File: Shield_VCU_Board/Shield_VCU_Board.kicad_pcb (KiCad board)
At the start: 2 copper layers, 250.5 x 110 mm, 148 parts, among them J1 Conn_02x08_Odd_Even, J10 Main_Supply, J11 Conn_01x40_Socket, J13 Conn_Molex_TouchPanel, J14 CAN_OUT, J15 Conn_01x04_Socket, J2 Conn_02x10_Odd_Even, J3/1 NXP3, J4 Conn_02x08_Odd_Even, J5 Conn_02x10_Odd_Even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

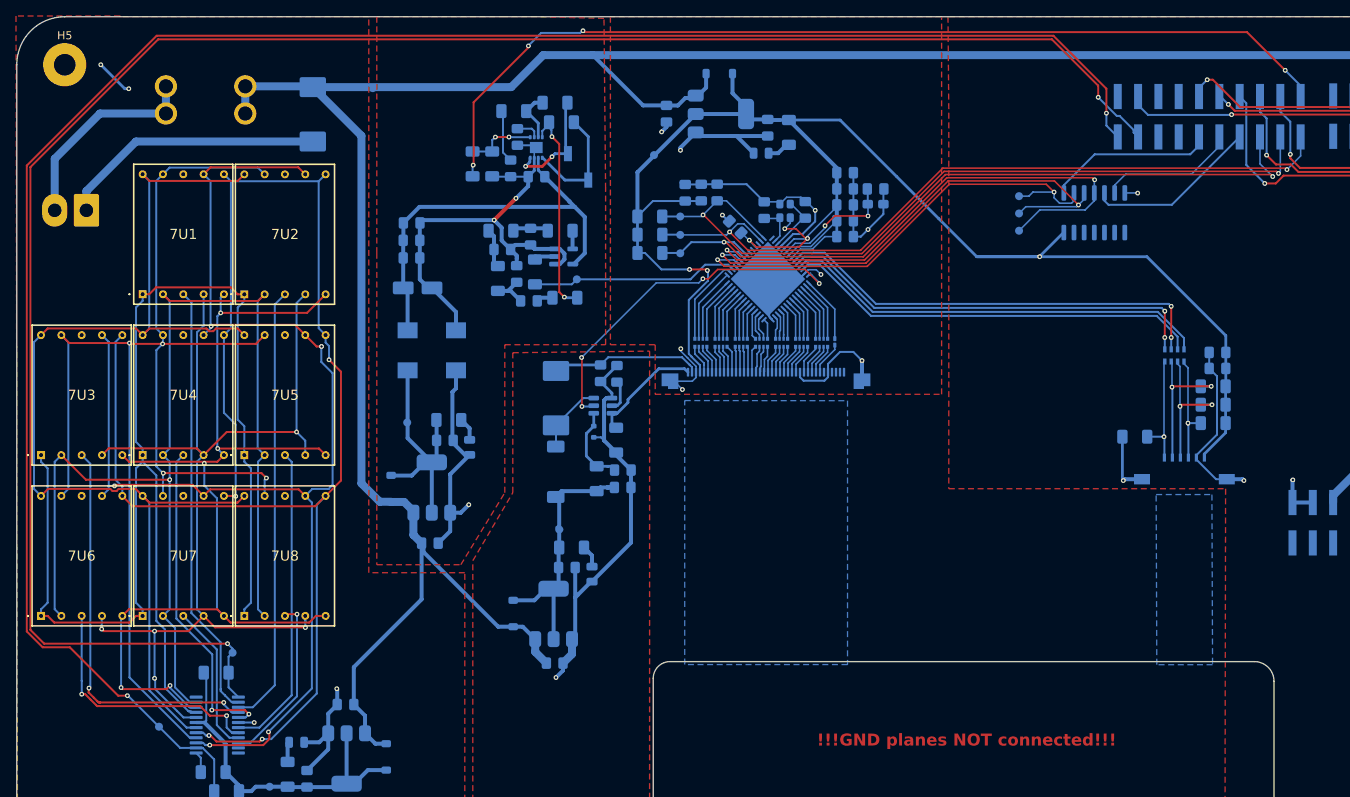
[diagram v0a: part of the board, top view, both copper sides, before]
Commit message: Wire routing_small change
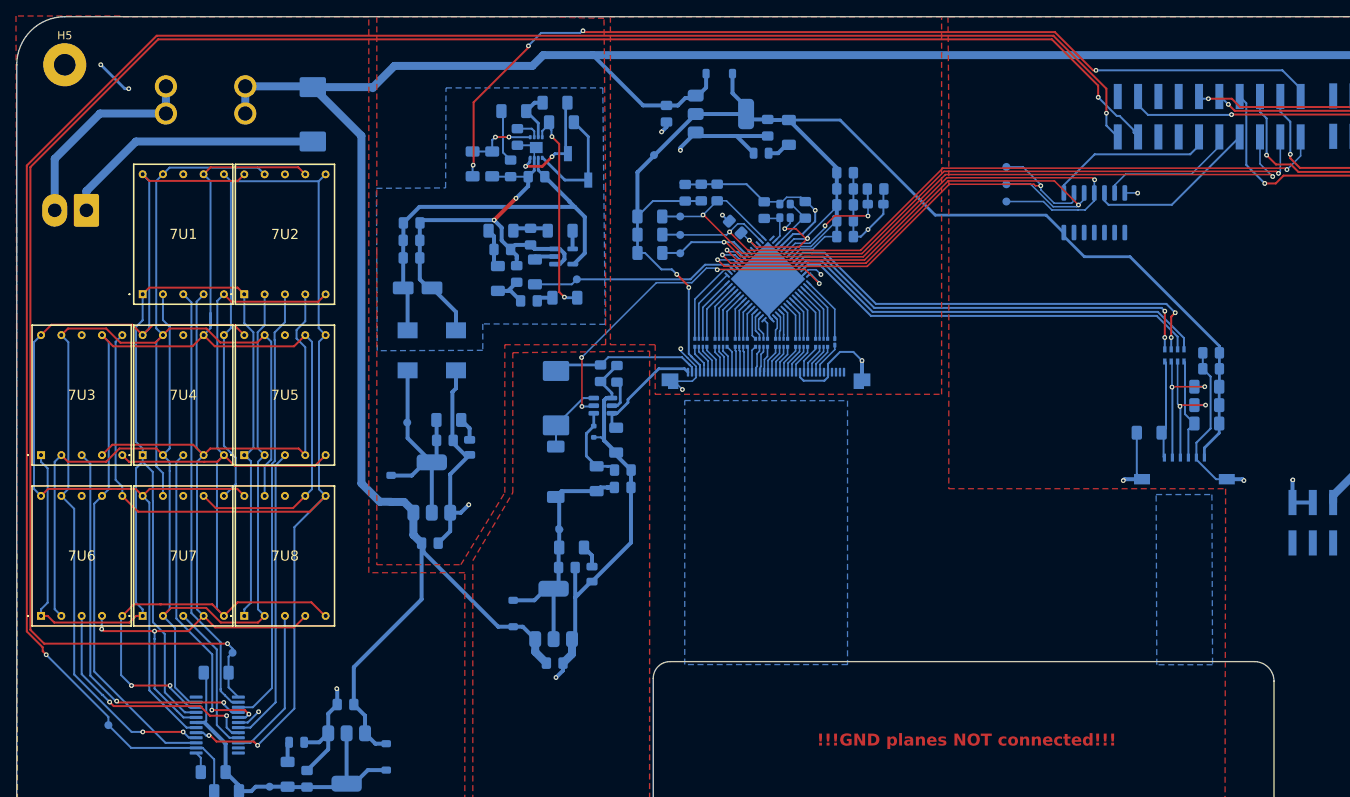
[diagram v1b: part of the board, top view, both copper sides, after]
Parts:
- moved SCL7 6.33 mm to (36.5, 132.6)
- moved MISO1 3.98 mm to (148.7, 64.9)
- moved MOSI1 3.98 mm to (148.7, 67.1)
- moved SCK1 3.98 mm to (148.7, 62.8)
- moved R62 1.87 mm to (166.6, 96.0)
- moved C16 0.80 mm to (174.3, 86.0)
- moved C41 0.80 mm to (174.3, 88.0)
- moved R61 0.80 mm to (173.8, 94.8)
- moved R63 0.80 mm to (173.8, 92.5)
- moved R64 0.80 mm to (173.8, 90.2)
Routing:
- net 3V3_DSPL: track 222.5 -> 204.2 mm, vias 6 -> 5
- net Net-(7U1-F): track 170.9 -> 166.5 mm, vias 4 -> 2
- net Net-(7U1-A): track 160.5 -> 158.0 mm, vias 5 -> 0
- net Net-(U1-DIG7): track 21.6 -> 19.2 mm, vias 1 -> 0
- net FT_MISO: track 62.8 -> 65.2 mm
- net Net-(J2-Pin_12): track 172.4 -> 170.1 mm
- net Net-(J13-Pin_6): track 14.2 -> 12.4 mm, vias 1 -> 0
- net Net-(U1-DIG2): track 50.1 -> 48.6 mm
- net Net-(U1-DIG5): track 32.3 -> 30.9 mm
- net Net-(7U1-B): track 187.0 -> 185.6 mm, vias 4 -> 2
- net Net-(U1-DIG4): track 38.7 -> 37.3 mm
- net GND: track 295.3 -> 296.6 mm
- net Net-(J13-Pin_3): track 13.8 -> 12.9 mm, vias 1 -> 0
- net FT_MOSI: track 67.0 -> 67.9 mm
- net 7S_NXP_SCL: track 244.7 -> 245.6 mm
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- added copper zone on B.Cu, net GNDA

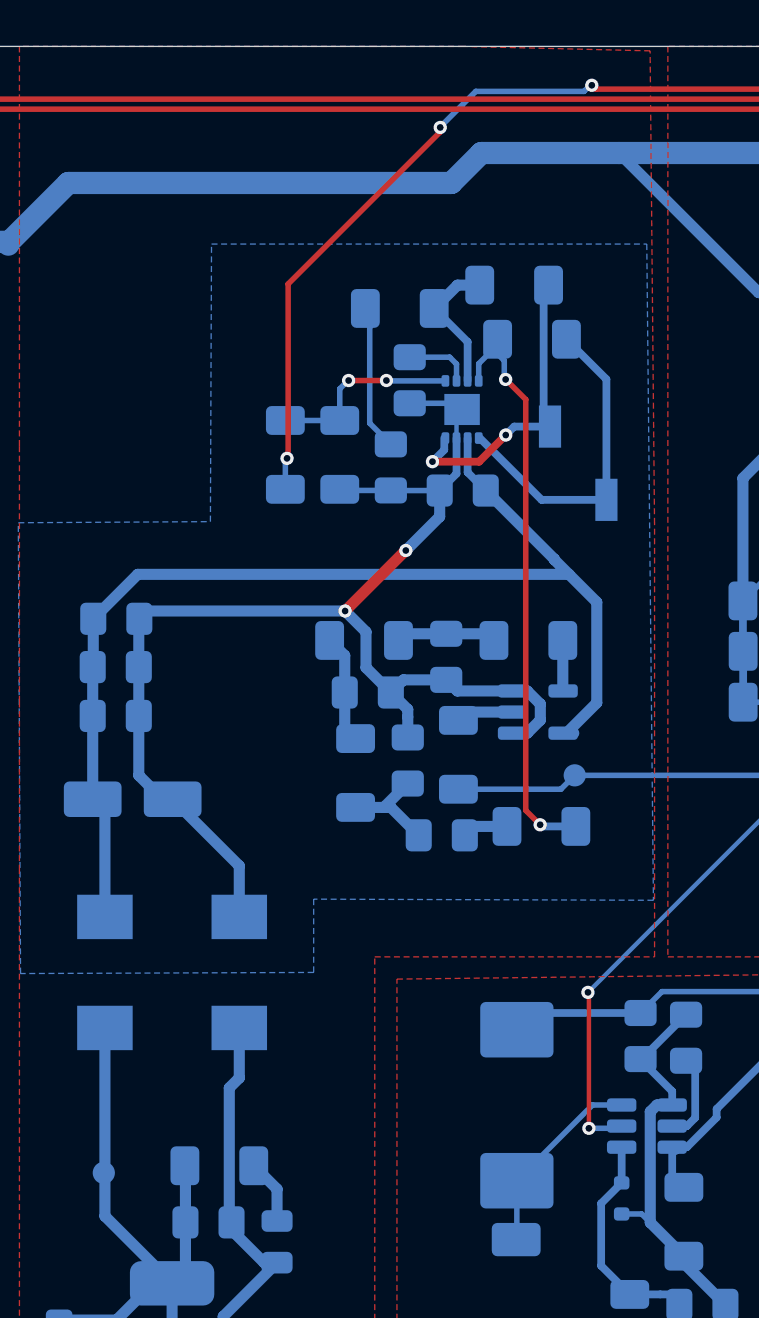
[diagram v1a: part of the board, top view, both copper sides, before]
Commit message: GNDA plane added(proto)
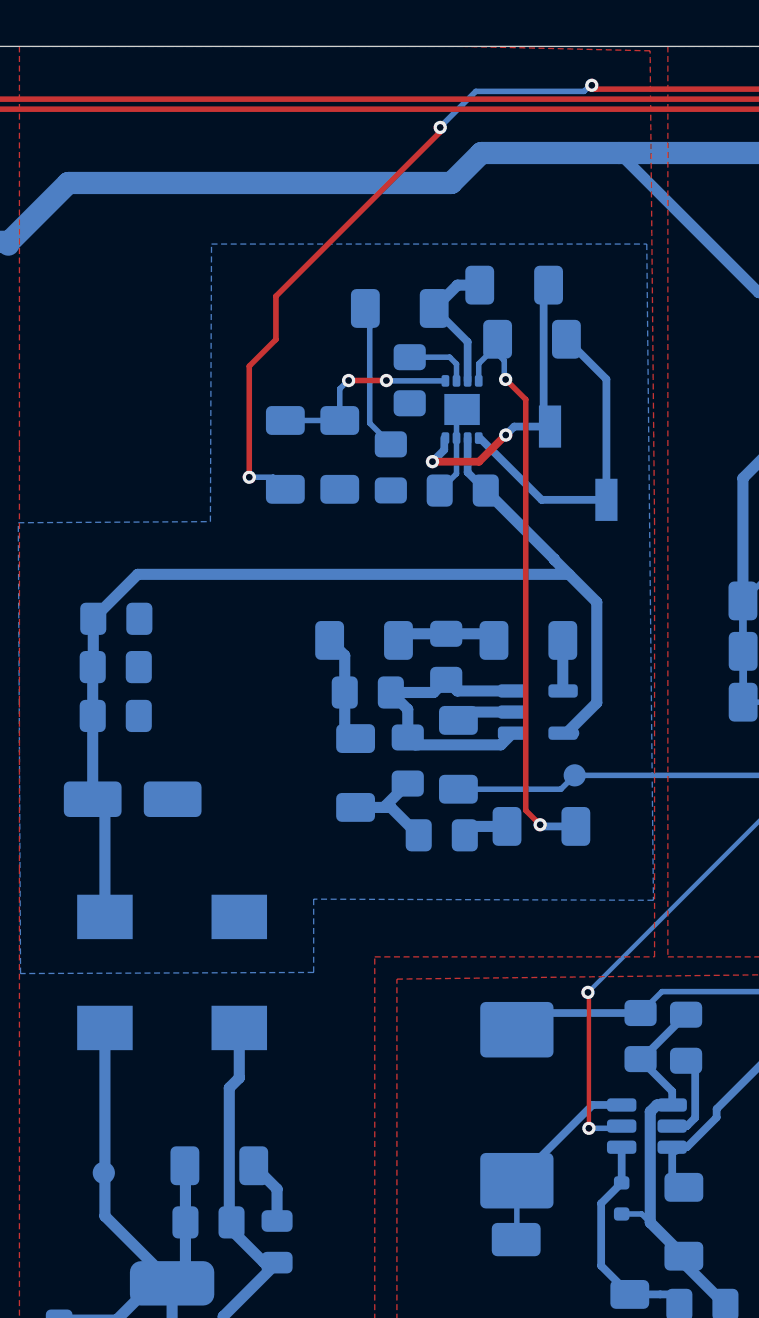
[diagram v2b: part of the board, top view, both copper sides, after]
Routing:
- net GNDA: track 60.7 -> 17.4 mm, vias 2 -> 0
- net AUD_SHDN: track 120.7 -> 122.7 mm

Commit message: Audio rotate+ GNDA plane separate
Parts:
- moved J8 13.4 mm to (82.8, 67.9), turned to 0 degrees
- moved R13 10.4 mm to (90.8, 65.0), turned to 90 degrees
- moved R8 10.2 mm to (87.3, 80.8), turned to 90 degrees
- moved R15 9.87 mm to (88.3, 65.8), turned to 90 degrees
- moved C11 9.49 mm to (82.0, 75.4), turned to 90 degrees
- moved R9 9.31 mm to (93.3, 81.2), turned to 180 degrees
- moved C2 8.54 mm to (89.7, 80.7), turned to 90 degrees
- moved C6 8.54 mm to (81.5, 62.7), turned to -90 degrees
- moved R10 7.75 mm to (83.1, 54.7), turned to 180 degrees
- moved C42 7.42 mm to (96.1, 77.3), turned to 90 degrees
- moved R14 6.67 mm to (95.7, 72.8), turned to 90 degrees
- moved C10 6.47 mm to (79.8, 75.4), turned to 90 degrees
- moved R7 6.19 mm to (87.3, 73.4), turned to 90 degrees
- moved C3 5.90 mm to (92.7, 78.9), turned to 180 degrees
- moved C1 5.75 mm to (88.1, 77.1), turned to 0 degrees
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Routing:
- net GNDA: track 17.4 -> 49.0 mm, vias 0 -> 2
- net Net-(U4-IN-): track 26.5 -> 13.7 mm, vias 2 -> 0
- net AUD_SHDN: track 122.7 -> 112.4 mm, vias 4 -> 3
- net 3V3_SPKR: track 52.5 -> 44.6 mm
- net Audio_L: track 26.6 -> 22.5 mm
- net GND: track 296.6 -> 294.6 mm, vias 21 -> 20
- added copper zone on F.Cu, net GNDA
- removed copper zone on B.Cu, net GNDA

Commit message: Required_corr_0.1
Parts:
- moved SCK1 7.12 mm to (147.2, 69.8)
- moved C13 5.53 mm to (128.5, 71.4)
- moved C12 5.53 mm to (128.5, 69.5)
- moved AUDV3.3 4.91 mm to (77.5, 91.5)
- moved C17 3.99 mm to (128.5, 67.5)
- moved C19 3.99 mm to (128.5, 63.5)
- moved C36 3.99 mm to (128.5, 65.5)
- moved C37 3.99 mm to (128.5, 59.5)
- moved C7 3.99 mm to (128.5, 61.5)
- moved MISO1 3.32 mm to (149.0, 68.2)
- moved MOSI1 2.08 mm to (150.8, 66.8)
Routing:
- net FT_MOSI: track 67.9 -> 56.1 mm, vias 2 -> 3
- net FT_MISO: track 65.2 -> 54.7 mm, vias 2 -> 3
- net 3V3_DSPL: track 204.3 -> 211.8 mm, vias 5 -> 7
- net +1V2: track 15.7 -> 9.96 mm, vias 2 -> 0
- net FT_PD: track 98.7 -> 93.3 mm, vias 2 -> 3
- net 3V3_AUD: track 30.4 -> 25.3 mm
- net FT_T_SCK: track 59.7 -> 55.0 mm, vias 2 -> 3
- net GND: track 294.6 -> 291.4 mm
- net 7S_NXP_SCL: track 245.6 -> 247.9 mm
- net LED2_PTA12: track 93.3 -> 92.7 mm
- net AUD_SHDN: track 112.4 -> 111.9 mm
- net BL_PWM: track 45.2 -> 45.7 mm

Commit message: Required_corr_0.2
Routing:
- net BL_PWM: track 45.7 -> 56.2 mm

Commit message: Required_corr_0.3
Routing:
- net +12V: track 409.2 -> 428.0 mm

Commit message: Required_corr_0.4
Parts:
- moved SDA7 23.6 mm to (33.0, 137.5), turned to 90 degrees
- moved R55 19.2 mm to (38.2, 141.3), turned to 90 degrees
- moved R56 10.5 mm to (40.8, 139.7), turned to 90 degrees
- moved RSET1 7.76 mm to (46.1, 131.5)
- moved U1 5.87 mm to (47.6, 137.9), turned to 90 degrees
- moved C31 2.98 mm to (67.8, 132.4)
- moved C32 2.98 mm to (63.0, 141.7)
- moved U8 2.98 mm to (67.9, 139.2)
- moved D12 2.98 mm to (61.7, 137.2)
- moved R52 2.98 mm to (60.5, 141.2)
- moved D9 2.98 mm to (72.9, 139.0)
- moved SEGV3.3 2.98 mm to (58.3, 142.7)
- moved SCL7 2.49 mm to (36.0, 135.0), turned to 90 degrees
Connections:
- 7U1 pad 3: Net-(U1-DIG0) -> Net-(U1-DIG4)
- 7U2 pad 3: Net-(U1-DIG1) -> Net-(U1-DIG2)
- 7U3 pad 3: Net-(U1-DIG2) -> Net-(U1-DIG7)
- 7U4 pad 3: Net-(U1-DIG3) -> Net-(U1-DIG5)
- 7U5 pad 3: Net-(U1-DIG4) -> Net-(U1-DIG1)
- 7U6 pad 3: Net-(U1-DIG5) -> Net-(U1-DIG6)
- 7U7 pad 3: Net-(U1-DIG6) -> Net-(U1-DIG3)
- 7U8 pad 3: Net-(U1-DIG7) -> Net-(U1-DIG0)
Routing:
- net Net-(U1-DIG0): track 54.3 -> 25.0 mm, vias 0 -> 1
- net Net-(U1-DIG7): track 19.2 -> 47.4 mm, vias 0 -> 2
- net Net-(U1-DIG4): track 37.3 -> 63.8 mm, vias 0 -> 2
- net Net-(7U1-G): track 141.9 -> 161.8 mm, vias 0 -> 3
- net Net-(7U1-DP): track 129.1 -> 147.8 mm, vias 2 -> 0
- net 3V3_7seg: track 43.7 -> 61.8 mm
- net Net-(U1-DIG3): track 40.4 -> 22.8 mm
- net Net-(U1-DIG2): track 48.6 -> 65.8 mm
- net Net-(7U1-E): track 166.1 -> 150.1 mm, vias 0 -> 1
- net Net-(7U1-B): track 185.6 -> 169.9 mm
- net Net-(7U1-C): track 132.9 -> 147.8 mm, vias 2 -> 0
- net Net-(U1-DIG5): track 30.9 -> 43.3 mm
- net Net-(7U1-A): track 158.0 -> 167.8 mm
- net Net-(U1-DIG6): track 18.7 -> 27.7 mm, vias 0 -> 2
- net Net-(U1-DIG1): track 55.1 -> 46.4 mm, vias 0 -> 2
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
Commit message: Required_corr_0.5
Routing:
- net 7S_NXP_SDA: track 249.9 -> 256.4 mm
- net GND: track 289.8 -> 284.5 mm, vias 20 -> 18
- net AUD_SHDN: track 111.9 -> 107.3 mm, vias 3 -> 2
- net +12V: track 430.3 -> 427.4 mm
